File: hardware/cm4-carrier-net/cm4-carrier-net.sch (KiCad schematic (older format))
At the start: 42 parts, among them J1 USB_C_Receptacle_USB2.0, J2 Micro_SD_Card, J3 Abracon_ARJM11-502, Q1 DMP2066LSN, SW1 BOOT, SW2 GLOBAL_EN, U5 Compute_Module_4_Functional, U6 TPD2EUSB30

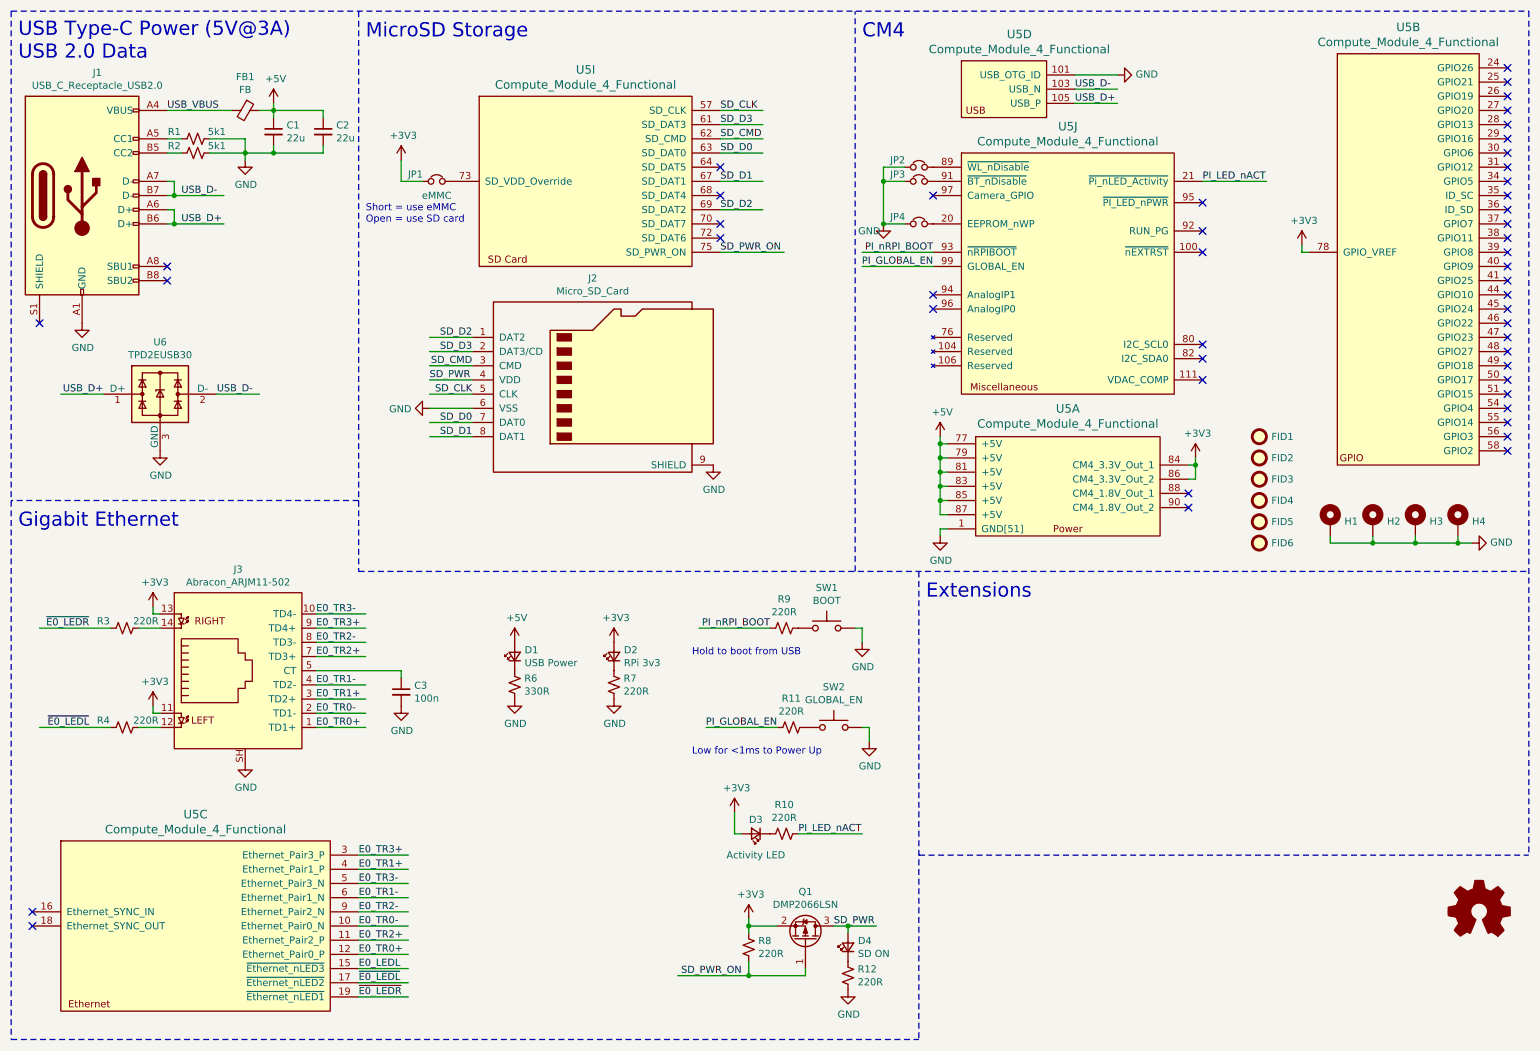
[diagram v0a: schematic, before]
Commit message: Added USB OTG ID selection switch. Likely finalized v1.0a.
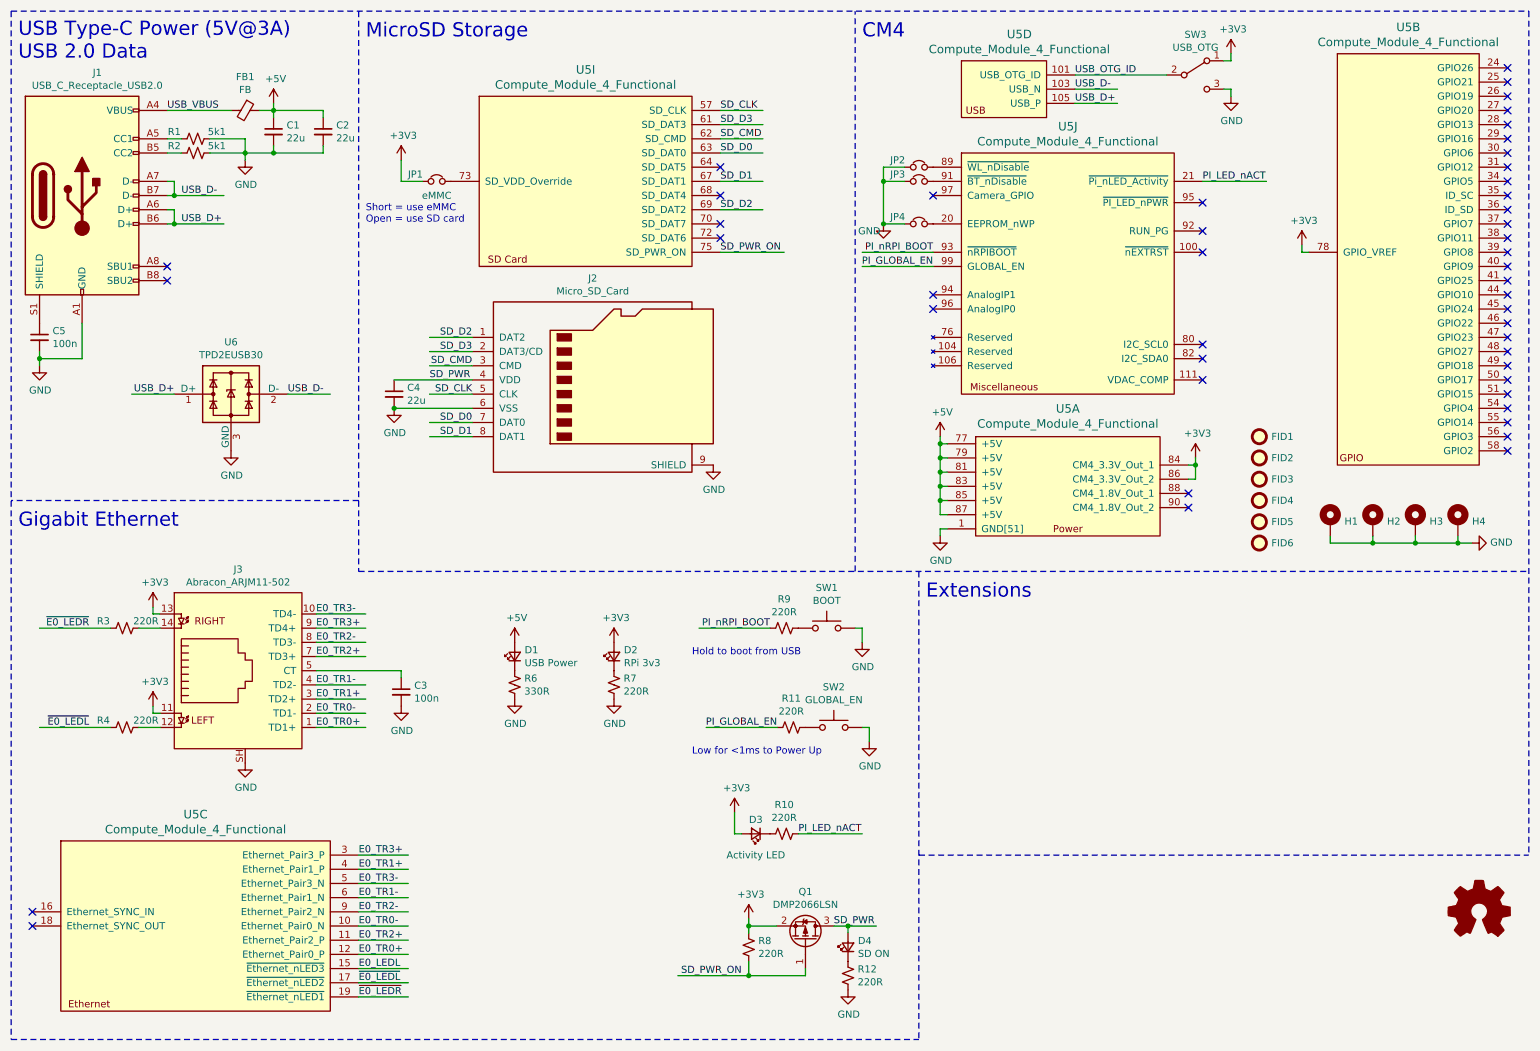
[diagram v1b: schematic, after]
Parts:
- added C4: 22u, Capacitor_SMD:C_0805_2012Metric, symbol Device:C_Small
- added C5: 100n, Capacitor_SMD:C_0805_2012Metric, symbol Device:C_Small
- added SW3: USB_OTG, Button_Switch_SMD:SW_SPDT_CK-JS102011SAQN, symbol Switch:SW_SPDT
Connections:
- net labels added: USB_OTG_ID
- wire segments 130 -> 138
- no-connect marks 48 -> 47
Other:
- moved on the sheet: U6
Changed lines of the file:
@@
-	1    0    0    -1
-$EndComp
-$Comp
-L Connector:USB_C_Receptacle_USB2.0 J1
-U 1 1 613A5B0A
-P 1000 1800
-F 0 "J1" H 1107 2667 50  0000 C CNN
-F 1 "USB_C_Receptacle_USB2.0" H 1107 2576 50  0000 C CNN
-F 2 "jkiv-library:USB_C_Receptacle_GCT-USB4105" H 1150 1800 50  0001 C CNN
-F 3 "https://www.usb.org/sites/default/files/documents/usb_type-c.zip" H 1150 1800 50  0001 C CNN
-	1    1000 1800
 	1    0    0    -1
 $EndComp
 NoConn ~ 1600 2300
 NoConn ~ 1600 2400
-NoConn ~ 700  2700
 $Comp
 L Device:R_Small_US R1
@@
 Text Label 3750 3000 2    50   ~ 0
 SD_CMD
-$Comp
-L power:GND #PWR0114
-U 1 1 613FBAE3
-P 3450 3300
-F 0 "#PWR0114" H 3450 3050 50  0001 C CNN
-F 1 "GND" V 3455 3172 50  0000 R CNN
-F 2 "" H 3450 3300 50  0001 C CNN
-F 3 "" H 3450 3300 50  0001 C CNN
-	1    3450 3300
-	0    1    1    0
-$EndComp
 Text Label 3750 3200 2    50   ~ 0
 SD_CLK
@@
 Wire Wire Line
 	3750 3200 3450 3200
-Wire Wire Line
-	3750 3300 3450 3300
 Wire Wire Line
 	3750 3400 3450 3400
@@
 L Power_Protection:TPD2EUSB30 U6
 U 1 1 61578F10
-P 1550 3200
-F 0 "U6" H 1550 3567 50  0000 C CNN
-F 1 "TPD2EUSB30" H 1550 3476 50  0000 C CNN
-F 2 "Package_TO_SOT_SMD:Texas_DRT-3" H 800 2900 50  0001 C CNN
-F 3 "http://www.ti.com/lit/ds/symlink/tpd2eusb30a.pdf" H 1550 3200 50  0001 C CNN
-	1    1550 3200
+P 2050 3200
+F 0 "U6" H 2050 3567 50  0000 C CNN
+F 1 "TPD2EUSB30" H 2050 3476 50  0000 C CNN
+F 2 "Package_TO_SOT_SMD:Texas_DRT-3" H 1300 2900 50  0001 C CNN
+F 3 "http://www.ti.com/lit/ds/symlink/tpd2eusb30a.pdf" H 2050 3200 50  0001 C CNN
+	1    2050 3200
 	1    0    0    -1
 $EndComp
@@
 L power:GND #PWR0107
 U 1 1 615AE28D
-P 1000 2700
-F 0 "#PWR0107" H 1000 2450 50  0001 C CNN
-F 1 "GND" H 1005 2527 50  0000 C CNN
-F 2 "" H 1000 2700 50  0001 C CNN
-F 3 "" H 1000 2700 50  0001 C CNN
-	1    1000 2700
+P 700 3000
+F 0 "#PWR0107" H 700 2750 50  0001 C CNN
+F 1 "GND" H 705 2827 50  0000 C CNN
+F 2 "" H 700 3000 50  0001 C CNN
+F 3 "" H 700 3000 50  0001 C CNN
+	1    700  3000
 	1    0    0    -1
 $EndComp
@@
 L power:GND #PWR0109
 U 1 1 615F04EE
-P 1550 3600
-F 0 "#PWR0109" H 1550 3350 50  0001 C CNN
-F 1 "GND" H 1555 3427 50  0000 C CNN
-F 2 "" H 1550 3600 50  0001 C CNN
-F 3 "" H 1550 3600 50  0001 C CNN
-	1    1550 3600
+P 2050 3600
+F 0 "#PWR0109" H 2050 3350 50  0001 C CNN
+F 1 "GND" H 2055 3427 50  0000 C CNN
+F 2 "" H 2050 3600 50  0001 C CNN
+F 3 "" H 2050 3600 50  0001 C CNN
+	1    2050 3600
 	1    0    0    -1
 $EndComp
@@
 Wire Wire Line
 	2350 1500 2150 1500
-Text Label 1950 3200 0    50   ~ 0
+Text Label 2450 3200 0    50   ~ 0
 USB_D-
 Wire Wire Line
-	1950 3200 2250 3200
-Text Label 1150 3200 2    50   ~ 0
+	2450 3200 2750 3200
+Text Label 1650 3200 2    50   ~ 0
 USB_D+
 Wire Wire Line
-	1150 3200 850  3200
+	1650 3200 1350 3200
 Wire Notes Line
 	6900 4450 6900 7750
@@
 Wire Wire Line
 	2650 5150 3250 5150
-$Comp
-L power:GND #PWR0115
-U 1 1 617F991E
-P 8300 950
-F 0 "#PWR0115" H 8300 700 50  0001 C CNN
-F 1 "GND" V 8305 822 50  0000 R CNN
-F 2 "" H 8300 950 50  0001 C CNN
-F 3 "" H 8300 950 50  0001 C CNN
-	1    8300 950
-	0    -1   -1   0
-$EndComp
-Wire Wire Line
-	8300 950  8000 950
 Wire Wire Line
 	6650 1600 6650 1700
@@
 SD_PWR
 Wire Wire Line
-	3450 3100 3750 3100
-Wire Wire Line
 	6300 6950 6400 6950
 Wire Wire Line
@@
 	1    0    0    -1
 $EndComp
+$Comp
+L power:GND #PWR0114
+U 1 1 61473C68
+P 3200 3300
+F 0 "#PWR0114" H 3200 3050 50  0001 C CNN
+F 1 "GND" H 3205 3127 50  0000 C CNN
+F 2 "" H 3200 3300 50  0001 C CNN
+F 3 "" H 3200 3300 50  0001 C CNN
+	1    3200 3300
+	1    0    0    -1
+$EndComp
+$Comp
+L Device:C_Small C4
+U 1 1 61473DCC
+P 3200 3200
+F 0 "C4" H 3292 3246 50  0000 L CNN
+F 1 "22u" H 3292 3155 50  0000 L CNN
+F 2 "Capacitor_SMD:C_0805_2012Metric" H 3200 3200 50  0001 C CNN
+F 3 "~" H 3200 3200 50  0001 C CNN
+	1    3200 3200
+	1    0    0    -1
+$EndComp
+Wire Wire Line
+	3200 3100 3750 3100
+Wire Wire Line
+	3200 3300 3750 3300
+Connection ~ 3200 3300
+$Comp
+L Connector:USB_C_Receptacle_USB2.0 J1
+U 1 1 613A5B0A
+P 1000 1800
+F 0 "J1" H 1107 2667 50  0000 C CNN
+F 1 "USB_C_Receptacle_USB2.0" H 1107 2576 50  0000 C CNN
+F 2 "jkiv-library:USB_C_Receptacle_GCT-USB4105" H 1150 1800 50  0001 C CNN
+F 3 "https://www.usb.org/sites/default/files/documents/usb_type-c.zip" H 1150 1800 50  0001 C CNN
+	1    1000 1800
+	1    0    0    -1
+$EndComp
+Text Label 8000 950  0    50   ~ 0
+USB_OTG_ID
+$Comp
+L Device:C_Small C5
+U 1 1 614E16BC
+P 700 2800
+F 0 "C5" H 792 2846 50  0000 L CNN
+F 1 "100n" H 792 2755 50  0000 L CNN
+F 2 "Capacitor_SMD:C_0805_2012Metric" H 700 2800 50  0001 C CNN
+F 3 "~" H 700 2800 50  0001 C CNN
+	1    700  2800
+	1    0    0    -1
+$EndComp
+Wire Wire Line
+	700  3000 700  2950
+Wire Wire Line
+	700  2950 1000 2950
+Wire Wire Line
+	1000 2700 1000 2950
+Connection ~ 700  2950
+Wire Wire Line
+	700  2950 700  2900
+Wire Wire Line
+	9100 1100 9100 1050
+$Comp
+L power:GND #PWR0115
+U 1 1 616548E2
+P 9100 1100
+F 0 "#PWR0115" H 9100 850 50  0001 C CNN
+F 1 "GND" H 9105 927 50  0000 C CNN
+F 2 "" H 9100 1100 50  0001 C CNN
+F 3 "" H 9100 1100 50  0001 C CNN
+	1    9100 1100
+	1    0    0    -1
+$EndComp
+Wire Wire Line
+	9100 850  9050 850
+Wire Wire Line
+	9100 800  9100 850
+$Comp
+L power:+3V3 #PWR0128
+U 1 1 6159525D
+P 9100 800
+F 0 "#PWR0128" H 9100 650 50  0001 C CNN
+F 1 "+3V3" H 9115 973 50  0000 C CNN
+F 2 "" H 9100 800 50  0001 C CNN
+F 3 "" H 9100 800 50  0001 C CNN
+	1    9100 800
+	1    0    0    -1
+$EndComp
+Wire Wire Line
+	8000 950  8650 950
+$Comp
+L Switch:SW_SPDT SW3
+U 1 1 6173091F
+P 8850 950
+F 0 "SW3" H 8850 1235 50  0000 C CNN
+F 1 "USB_OTG" H 8850 1144 50  0000 C CNN
+F 2 "Button_Switch_SMD:SW_SPDT_CK-JS102011SAQN" H 8850 950 50  0001 C CNN
+F 3 "~" H 8850 950 50  0001 C CNN
+	1    8850 950
+	1    0    0    -1
+$EndComp
+Wire Wire Line
+	9100 1050 9050 1050
 $EndSCHEMATC
